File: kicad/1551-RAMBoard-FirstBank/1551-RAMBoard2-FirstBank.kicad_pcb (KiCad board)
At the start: 2 copper layers, 58.7 x 40.6 mm, 12 parts, among them J1 Conn_01x02_Male, U1 27C512, U2 74LS139, U3 KM62256CLP, U4_SOCKET1 27128

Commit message: moving to 1551
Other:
- board text added: "1551-RAMBOard][ v1.1 (c) IV 2024 Maciej Witkowiak, <ytm@elysium.pl>"
- board text removed: "1541-RAMBOard][ v1.1 (c) IV 2024 Maciej Witkowiak, <ytm@elysium.pl>"
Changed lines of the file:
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@@
   (paper "A4")
   (title_block
-    (title "1541-RAMBOard][")
+    (title "1551-RAMBOard][")
     (date "2024-04-20")
     (company "YTM Enterprises")
@@
     (descr "Through hole straight pin header, 1x02, 2.54mm pitch, single row")
     (tags "Through hole pin header THT 1x02 2.54mm single row")
-    (property "Sheetfile" "1541-RAMBoard2-FirstBank.kicad_sch")
+    (property "Sheetfile" "1551-RAMBoard2-FirstBank.kicad_sch")
     (property "Sheetname" "")
     (attr through_hole)
@@
     (descr "Mounting Hole 2.5mm, no annular")
     (tags "mounting hole 2.5mm no annular")
-    (property "Sheetfile" "1541-RAMBoard2-FirstBank.kicad_sch")
+    (property "Sheetfile" "1551-RAMBoard2-FirstBank.kicad_sch")
     (property "Sheetname" "")
     (attr exclude_from_pos_files)
@@
     (descr "Through hole straight pin header, 1x02, 2.54mm pitch, single row")
     (tags "Through hole pin header THT 1x02 2.54mm single row")
-    (property "Sheetfile" "1541-RAMBoard2-FirstBank.kicad_sch")
+    (property "Sheetfile" "1551-RAMBoard2-FirstBank.kicad_sch")
     (property "Sheetname" "")
     (attr through_hole)
@@
     (descr "28-lead though-hole mounted DIP package, row spacing 15.24 mm (600 mils), Socket, LongPads")
     (tags "THT DIP DIL PDIP 2.54mm 15.24mm 600mil Socket LongPads")
-    (property "Sheetfile" "1541-RAMBoard2-FirstBank.kicad_sch")
+    (property "Sheetfile" "1551-RAMBoard2-FirstBank.kicad_sch")
     (property "Sheetname" "")
     (attr through_hole)
@@
     (descr "28-lead though-hole mounted DIP package, row spacing 15.24 mm (600 mils), Socket, LongPads")
     (tags "THT DIP DIL PDIP 2.54mm 15.24mm 600mil Socket LongPads")
-    (property "Sheetfile" "1541-RAMBoard2-FirstBank.kicad_sch")
+    (property "Sheetfile" "1551-RAMBoard2-FirstBank.kicad_sch")
     (property "Sheetname" "")
     (attr through_hole)
@@
     (descr "Through hole straight pin header, 1x02, 2.54mm pitch, single row")
     (tags "Through hole pin header THT 1x02 2.54mm single row")
-    (property "Sheetfile" "1541-RAMBoard2-FirstBank.kicad_sch")
+    (property "Sheetfile" "1551-RAMBoard2-FirstBank.kicad_sch")
     (property "Sheetname" "")
     (attr through_hole)
@@
     (descr "16-lead though-hole mounted DIP package, row spacing 7.62 mm (300 mils), Socket, LongPads")
     (tags "THT DIP DIL PDIP 2.54mm 7.62mm 300mil Socket LongPads")
-    (property "Sheetfile" "1541-RAMBoard2-FirstBank.kicad_sch")
+    (property "Sheetfile" "1551-RAMBoard2-FirstBank.kicad_sch")
     (property "Sheetname" "")
     (attr through_hole)
@@
     (descr "Through hole straight pin header, 1x02, 2.54mm pitch, single row")
     (tags "Through hole pin header THT 1x02 2.54mm single row")
-    (property "Sheetfile" "1541-RAMBoard2-FirstBank.kicad_sch")
+    (property "Sheetfile" "1551-RAMBoard2-FirstBank.kicad_sch")
     (property "Sheetname" "")
     (attr through_hole)
@@
     (descr "Resistor, Axial_DIN0207 series, Axial, Horizontal, pin pitch=7.62mm, 0.25W = 1/4W, length*diameter=6.3*2.5mm^2, http://cdn-reichelt.de/documents/datenblatt/B400/1_4W%23YAG.pdf")
     (tags "Resistor Axial_DIN0207 series Axial Horizontal pin pitch 7.62mm 0.25W = 1/4W length 6.3mm diameter 2.5mm")
-    (property "Sheetfile" "1541-RAMBoard2-FirstBank.kicad_sch")
+    (property "Sheetfile" "1551-RAMBoard2-FirstBank.kicad_sch")
     (property "Sheetname" "")
     (attr through_hole)
@@
     (descr "Resistor, Axial_DIN0207 series, Axial, Horizontal, pin pitch=7.62mm, 0.25W = 1/4W, length*diameter=6.3*2.5mm^2, http://cdn-reichelt.de/documents/datenblatt/B400/1_4W%23YAG.pdf")
     (tags "Resistor Axial_DIN0207 series Axial Horizontal pin pitch 7.62mm 0.25W = 1/4W length 6.3mm diameter 2.5mm")
-    (property "Sheetfile" "1541-RAMBoard2-FirstBank.kicad_sch")
+    (property "Sheetfile" "1551-RAMBoard2-FirstBank.kicad_sch")
     (property "Sheetname" "")
     (attr through_hole)
@@
     (descr "28-lead though-hole mounted DIP package, row spacing 15.24 mm (600 mils), Socket, LongPads")
     (tags "THT DIP DIL PDIP 2.54mm 15.24mm 600mil Socket LongPads")
-    (property "Sheetfile" "1541-RAMBoard2-FirstBank.kicad_sch")
+    (property "Sheetfile" "1551-RAMBoard2-FirstBank.kicad_sch")
     (property "Sheetname" "")
     (attr through_hole)
@@
     (descr "Through hole straight pin header, 1x02, 2.54mm pitch, single row")
     (tags "Through hole pin header THT 1x02 2.54mm single row")
-    (property "Sheetfile" "1541-RAMBoard2-FirstBank.kicad_sch")
+    (property "Sheetfile" "1551-RAMBoard2-FirstBank.kicad_sch")
     (property "Sheetname" "")
     (attr through_hole)
@@
     (effects (font (size 0.7 0.7) (thickness 0.15)) (justify left mirror))
   )
-  (gr_text "1541-RAMBOard][ v1.1\n(c) IV 2024 Maciej Witkowiak, <ytm@elysium.pl>" (at 113.792 87.63 90) (layer "B.SilkS")
+  (gr_text "1551-RAMBOard][ v1.1\n(c) IV 2024 Maciej Witkowiak, <ytm@elysium.pl>" (at 113.792 87.63 90) (layer "B.SilkS")
     (effects (font (size 0.7 0.7) (thickness 0.15)) (justify left mirror))
   )

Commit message: first attempt
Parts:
- removed R14: 10K, Resistor_THT:R_Axial_DIN0207_L6.3mm_D2.5mm_P7.62mm_Horizontal
- removed ROM_A14: ROM_A14, Connector_PinHeader_2.54mm:PinHeader_1x02_P2.54mm_Vertical
- removed ROM_A15: ROM_A15, Connector_PinHeader_2.54mm:PinHeader_1x02_P2.54mm_Vertical
- added J2: Conn_01x03_Pin, Connector_PinHeader_2.54mm:PinHeader_1x03_P2.54mm_Vertical, F.Cu at (124.2, 124.2)
- added U4: 74LS00, Package_DIP:DIP-14_W7.62mm_Socket_LongPads, F.Cu at (119.4, 124.7)
- J1: value Conn_01x02_Male -> Conn_01x02_Pin
- RAM_A13: value RAM_A13 -> SolderJumper_2_Bridged; footprint Connector_PinHeader_2.54mm:PinHeader_1x02_P2.54mm_Vertical -> Jumper:SolderJumper-2_P1.3mm_Bridged_RoundedPad1.0x1.5mm
- RAM_A14: value RAM_A14 -> SolderJumper_2_Bridged; footprint Connector_PinHeader_2.54mm:PinHeader_1x02_P2.54mm_Vertical -> Jumper:SolderJumper-2_P1.3mm_Bridged_RoundedPad1.0x1.5mm
- moved H1 59.3 mm to (164.6, 125.0)
- moved J1 37.6 mm to (153.7, 124.2)
- moved RAM_A13 26.9 mm to (141.6, 126.2)
- moved RAM_A14 24.2 mm to (134.9, 126.2)
- moved U2 4.65 mm to (119.4, 106.2)
- moved R15 1.83 mm to (165.4, 112.8)
- moved U1 1.83 mm to (158.0, 120.7)
- moved U3 1.83 mm to (139.2, 120.7)
- moved U4_SOCKET1 1.83 mm to (161.6, 120.7)
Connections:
- J1 pad 1: /A14 -> Net-(J1-Pin_1)
- J1 pad 2: /R/~{W} -> GND
- R15 pad 2: Net-(R15-Pad2) -> Net-(J1-Pin_1)
- U1 pad 1: Net-(R15-Pad2) -> Net-(J1-Pin_1)
- U1 pad 27: Net-(R14-Pad1) -> /A14
- U4_SOCKET1 pad 22: /~{A15} -> unconnected-(U4_SOCKET1-~{OE}-Pad22)
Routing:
- net GND: track 75.4 -> 0.00 mm
- net /A14: track 72.3 -> 0.00 mm
- net VCC: track 66.8 -> 0.00 mm, vias 2 -> 0
- net Net-(R14-Pad1): track 47.8 -> 0.00 mm, vias 1 -> 0
- net /~{A15}: track 39.7 -> 0.00 mm
- net Net-(R15-Pad2): track 35.0 -> 0.00 mm
- net /~{ROMSEL}: track 31.6 -> 0.00 mm
- net /A13: track 30.0 -> 0.00 mm, vias 1 -> 0
- net Net-(RAM_A14-B): track 27.6 -> 0.00 mm, vias 1 -> 0
- net /VPP: track 25.3 -> 0.00 mm
- net /D1: track 23.9 -> 0.00 mm, vias 1 -> 0
- net /D2: track 23.8 -> 0.00 mm, vias 1 -> 0
- net /A3: track 23.5 -> 0.00 mm, vias 1 -> 0
- net /A12: track 23.5 -> 0.00 mm, vias 1 -> 0
- net /A2: track 23.4 -> 0.00 mm
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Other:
- board size 58.7 x 40.6 mm -> 58.7 x 42.4 mm
- board text added: "1551-RAMBOard][ v1.0 (c) XII 2025 Maciej Witkowiak, <ytm@elysium.pl>"
- board text added: "A13"
- board text added: "A14"
- board text added: "J1 selects 32K half of 64K ROM short: bottom half open: top half"
- board text added: "R/~{W} | A14 | A15"
- board text added: "RAM_A13/14 jumpers closed: GND for 8K opened: connect to ??? to have 8K banks"
- board text removed: "1551-RAMBOard][ v1.1 (c) IV 2024 Maciej Witkowiak, <ytm@elysium.pl>"
- board text removed: "GND"
- board text removed: "R/~{W} | A14"
- board text removed: "RAM_A13/14 jumpers closed: GND for 8K opened: connect to VIA#2 PA to have 8K banks"
- board text removed: "ROM_A14 closed: $A000-$FFFF is ROM, omit R14 open: $C000-$FFFF is ROM, install R14 and switch between round pad and GND ROM_A15 closed: 32K ROM or upper half or 64K ROM, omit R15 open: install R15 and switch between round pad and GND"

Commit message: first try
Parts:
- removed H1: MountingHole, MountingHole:MountingHole_2.5mm
- moved U2 70.6 mm to (190.0, 104.6)
- moved U4 70.6 mm to (190.0, 123.2)
- moved J2 69.4 mm to (193.5, 120.7), turned to 180 degrees
- moved J1 45.6 mm to (193.5, 102.1), turned to 0 degrees
- moved U3 39.4 mm to (178.6, 119.9)
- moved RAM_A13 32.8 mm to (174.4, 123.7)
- moved RAM_A14 32.8 mm to (167.6, 123.7)
- moved R15 20.4 mm to (148.1, 123.7), turned to 0 degrees
- moved U1 2.41 mm to (155.7, 119.9)
- moved U4_SOCKET1 2.41 mm to (159.4, 119.9)
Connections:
- U4_SOCKET1 pad 1: /VPP -> unconnected-(U4_SOCKET1-VPP-Pad1)
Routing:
- net GND: track 0.00 -> 103.0 mm, vias 0 -> 2
- net VCC: track 0.00 -> 80.5 mm, vias 0 -> 1
- net /A14: track 0.00 -> 77.6 mm, vias 0 -> 1
- net /~{A15}: track 0.00 -> 67.3 mm
- net /A13: track 0.00 -> 55.4 mm, vias 0 -> 2
- net Net-(J1-Pin_1): track 0.00 -> 50.8 mm, vias 0 -> 3
- net /~{ROMSEL}: track 0.00 -> 45.1 mm
- net /R/~{W}: track 0.00 -> 31.6 mm
- net /~{RAMSEL}: track 0.00 -> 28.7 mm
- net /D1: track 0.00 -> 24.3 mm, vias 0 -> 1
- net /A12: track 0.00 -> 23.9 mm
- net /A1: track 0.00 -> 23.8 mm
- net /D7: track 0.00 -> 23.8 mm
- net /A11: track 0.00 -> 23.8 mm
- net /A9: track 0.00 -> 23.8 mm
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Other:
- board size 58.7 x 42.4 mm -> 58.7 x 40.6 mm
- board text added: "J1: short: bottom 32K of 64K ROM open: top 32K of 64K ROM"
- board text added: "J2: - A14 from CPU (U2) pin 21 or U7 pin 7 - A15 from CPU (U2) pin 22 or U7 pin 6 - R/~{W} from onboard RAM (U5) pin 21 or or gate array (U6) pin 31(?) or U3 pin 19(?)"
- board text added: "RAM_A13/14 jumpers closed: GND for one 8K bank opened: connect to ??? to select one of four 8K banks"
- board text removed: "J1 A14 from CPU (U3) pin 24 R/~{W} from onboard RAM (U5) pin 21"
- board text removed: "J1 selects 32K half of 64K ROM short: bottom half open: top half"
- board text removed: "RAM_A13/14 jumpers closed: GND for 8K opened: connect to ??? to have 8K banks"

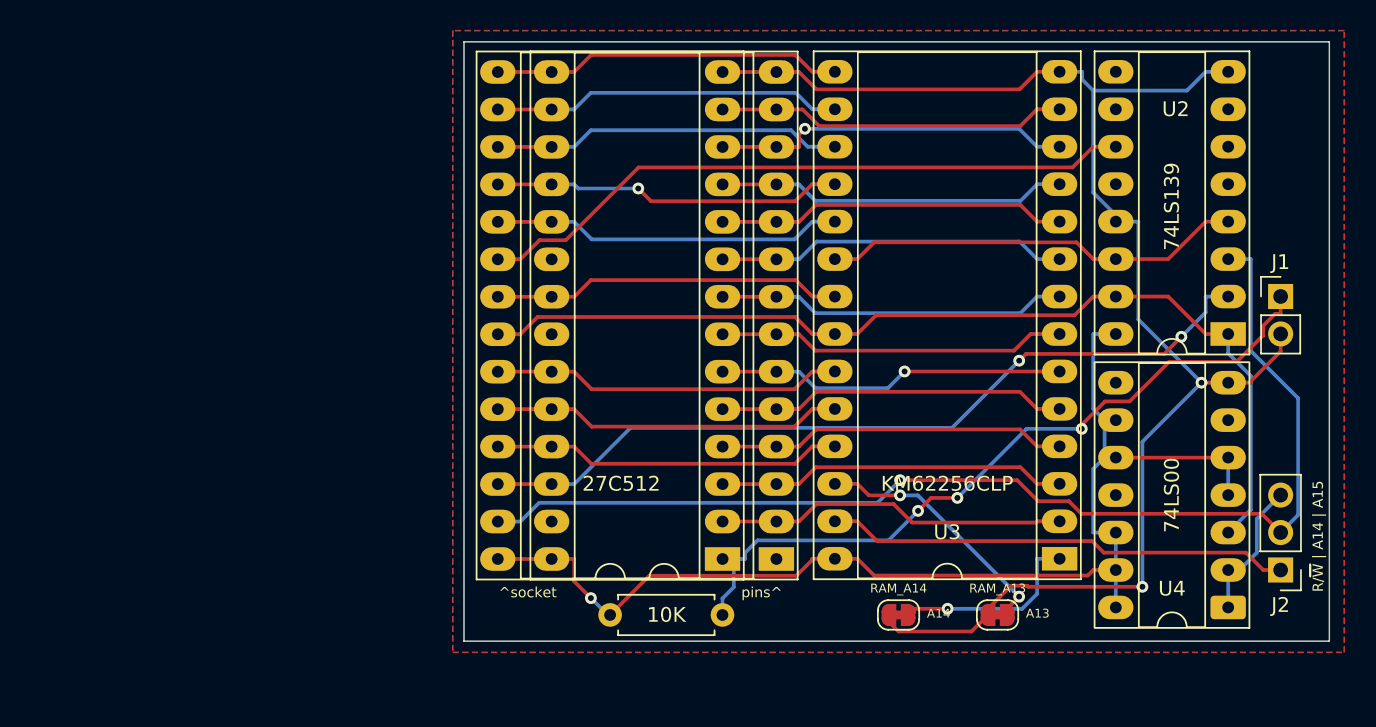
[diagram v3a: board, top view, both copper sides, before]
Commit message: final touches, support for 6264 (8K) and 62256 (32K)
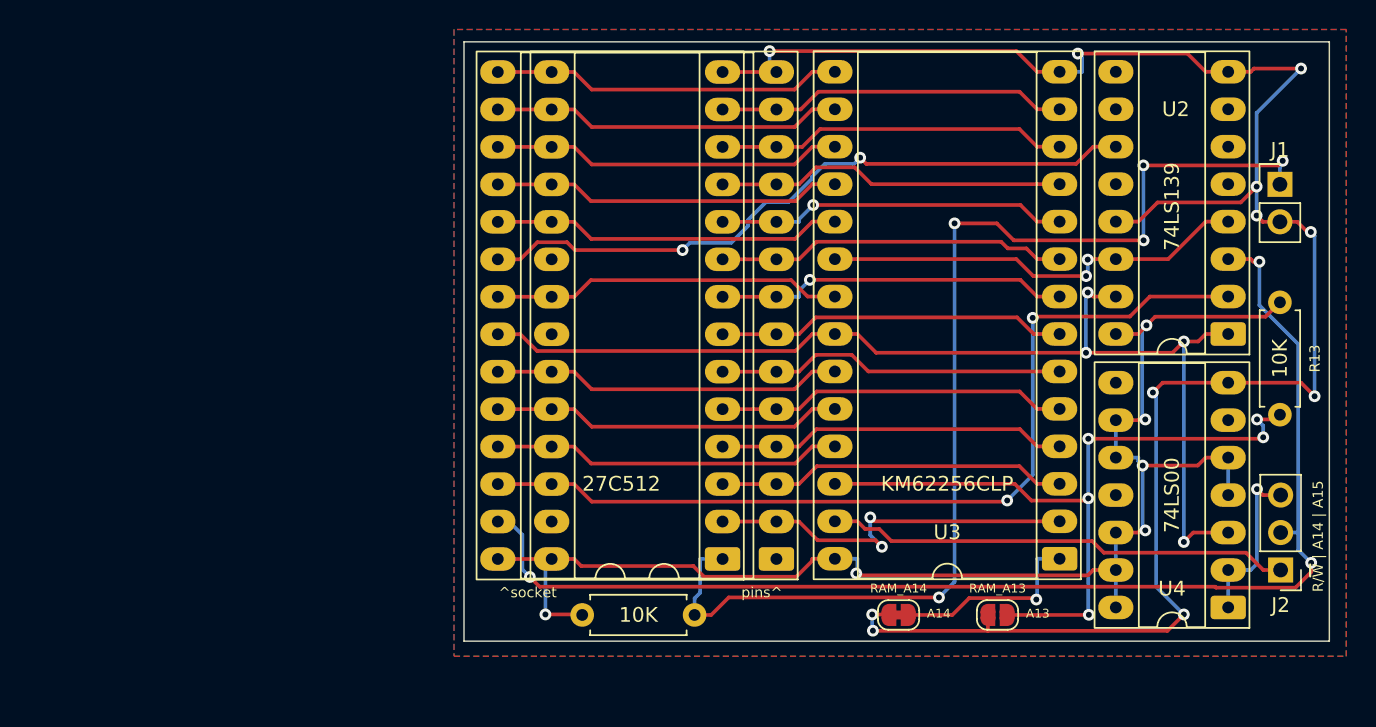
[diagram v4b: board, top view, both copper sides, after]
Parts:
- added R13: 10K, Resistor_THT:R_Axial_DIN0207_L6.3mm_D2.5mm_P7.62mm_Horizontal, F.Cu at (193.5, 102.5)
- RAM_A13: value SolderJumper_2_Bridged -> SolderJumper_2_Open; footprint Jumper:SolderJumper-2_P1.3mm_Bridged_RoundedPad1.0x1.5mm -> Jumper:SolderJumper-2_P1.3mm_Open_RoundedPad1.0x1.5mm
- moved J1 7.60 mm to (193.5, 94.5)
- moved R15 1.89 mm to (146.2, 123.7)
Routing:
- net Net-(RAM_A13-B): track 17.2 -> 50.2 mm, vias 2 -> 5
- net GND: track 103.0 -> 133.7 mm, vias 2 -> 11
- net Net-(J1-Pin_1): track 50.8 -> 78.0 mm, vias 3 -> 5
- net VCC: track 80.5 -> 96.3 mm, vias 1 -> 6
- net /~{A15}: track 67.3 -> 74.5 mm, vias 0 -> 4
- net /A14: track 77.6 -> 84.7 mm, vias 1 -> 3
- net /A13: track 55.4 -> 62.0 mm
- net /A12: track 23.9 -> 26.8 mm, vias 0 -> 2
- net /A15: track 9.86 -> 11.8 mm, vias 0 -> 1
- net /~{ROMSEL}: track 45.1 -> 46.2 mm, vias 0 -> 2
- net /~{RAMSEL}: track 28.7 -> 29.3 mm, vias 0 -> 2
- net /D1: track 24.3 -> 23.9 mm, vias 1 -> 0
- net /A2: track 23.8 -> 24.0 mm, vias 0 -> 1
- net /A0: track 23.8 -> 23.9 mm, vias 0 -> 1
- net /A4: vias 1 -> 0
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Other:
- board text added: "RAM_A13: open for 6264 (with R13 pullup) RAM_A14: closed 62256: like for 6264 or opened and connected to ??? to select one of four 8K banks"
- board text removed: "RAM_A13/14 jumpers closed: GND for one 8K bank opened: connect to ??? to select one of four 8K banks"

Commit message: updates after real hardware test, clarify R/W connection info
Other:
- board text added: "J2: - A14 from CPU (U2) pin 21 or U7 pin 7 - A15 from CPU (U2) pin 22 or U7 pin 6 - R/~{W} from onboard RAM (U5) pin 21 or or U3 pin 19"
- board text removed: "J2: - A14 from CPU (U2) pin 21 or U7 pin 7 - A15 from CPU (U2) pin 22 or U7 pin 6 - R/~{W} from onboard RAM (U5) pin 21 or or gate array (U6) pin 31(?) or U3 pin 19(?)"
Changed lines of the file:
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@@
 			"AAAAAAAAAAAAAAAAAAAAAAAAAAAAAAAAAAAAAAAAAAAAAAAAAAAAAAAAAAAAAAAAAAAAAAAAAAAA"
 			"AAAAAAAAAAAAAAAAAAAAAAAAAAAAAAAAAAAAAAAAAAAAAAAAAAAAAAAAAAAAAAAAAAAAAAAAAAAA"
-			"AAA="
+			"AAAAAAAAAAAAAAAAAAAAAAAAAAAAAAAAAAAAAAAAAAAAAAAAAAAAAAAAAAAAAAAAAAAAAAAAAAAA"
+			"AAAAAAAAAAAAAAAAAAAAAAAAAAAAAAAAAAAAAAAAAAAAAAAAAAAAAAAAAAAAAAAAAAAAAAAAAAAA"
+			"AAAAAAAAAAAAAAAAAAAAAAAAAAAAAAAAAAAAAAAAAAAAAAAAAAAAAAAAAAAAAAAAAAAAAAAAAAAA"
+			"AAAAAAAAAAAAAAAAAAAAAAAAAAAAAAAAAAAAAAAAAAAAAAAAAAAAAAAAAAAAAAAAAAAAAAAAAAAA"
+			"AAAAAAAAAAAAAAAAAAAAAAAAAAAAAAAAAAAAAAAAAAAAAAAAAAAAAAAAAAAAAAAAAAAAAAAAAAAA"
+			"AAAAAAAAAAAAAAAAAAAAAAAAAAAAAAAAAAAAAAAAAAAAAAAAAAAAAAAAAAAAAAAAAAAAAAAAAAAA"
+			"AAAAAAAAAAAAAAAAAAAAAAAAAAAAAAAAAAAAAAAAAAAAAAAAAAAAAAAAAAAAAAAAAAAAAAAAAAAA"
+			"AAAAAAAAAAAAAAAAAAAAAAAAAAAAAAAAAAAAAAAAAAAAAAAAAAAAAAAAAAAAAAAAAAAAAAAAAAAA"
+			"AAAAAAAAAAAAAAAAAAAAAAAAAAAAAAAAAAAAAAAAAAAAAAAAAAAAAAAAAAAAAAAAAAAAAAAAAAAA"
+			"AAAAAAAAAAAAAAAAAAAAAAAAAAAAAAAAAAAAAAAAAAAAAAAAAAAAAAAAAAAAAAAAAAAAAAAAAAAA"
+			"AAAAAAAAAAAAAAAAAAAAAAAAAAAAAAAAAAAAAAAAAAAAAAAAAAAAAAAAAAAAAAAAAAAAAAAAAAAA"
+			"AAAAAAAAAAAAAAAAAAAAAAAAAAAAAAAAAAAAAAAAAAAAAAAAAAAAAAAAAAAAAAAAAAAAAAAAAAAA"
+			"AAAAAAAAAAAAAAAAAAAAAAAAAAAAAAAAAAAAAAAAAAAAAAAAAAAAAAAAAAAAAAAAAAAAAAAAAAAA"
+			"AAAAAAAAAAAAAAAAAAAAAAAAAAAAAAAAAAAAAAAAAAAAAAAAAAAAAAAAAAAAAAAAAAAAAAAAAAAA"
+			"AAAAAAAAAAAAAAAAAAAAAAAAAAAAAAAAAAAAAAAAAAAAAAAAAAAAAAAAAAAAAAAAAAAAAAAAAAAA"
+			"AAAAAAAAAAAAAAAAAAAAAAAAAAAAAAAAAAAAAAAAAAAAAAAAAAAAAAAAAAAAAAAAAAAAAAAAAAAA"
+			"AAAAAAAAAAAAAAAAAAAAAAAAAAAAAAAAAAAAAAAAAAAAAAAAAAAAAAAAAAAAAAAAAAAAAAAAAAAA"
+			"AAAAAAAAAAAAAAAAAAAAAAAAAAAAAAAAAAAAAAAAAAAAAAAAAAAAAAAAAAAAAAAAAAAAAAAAAAAA"
+			"AA=="
 		)
 	)
@@
 		)
 	)
-	(gr_text "J2:\n- A14 from CPU (U2) pin 21 or U7 pin 7\n- A15 from CPU (U2) pin 22 or U7 pin 6\n- R/~{W} from onboard RAM (U5) pin 21 or\n  or gate array (U6) pin 31(?)\n  or U3 pin 19(?)"
+	(gr_text "J2:\n- A14 from CPU (U2) pin 21 or U7 pin 7\n- A15 from CPU (U2) pin 22 or U7 pin 6\n- R/~{W} from onboard RAM (U5) pin 21 or\n  or U3 pin 19"
 		(at 149.606 86.36 90)
 		(layer "B.SilkS")
